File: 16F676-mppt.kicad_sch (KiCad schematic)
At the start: 50 parts, among them J1 S+, J2 S-, J3 VB+, J4 VB-, Q1 BUK9511-55A127, Q2 BUK9511-55A127, Q3 2N2222A, Q4 2N2222A, Q5 2N2907A, Q6 2N2222A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

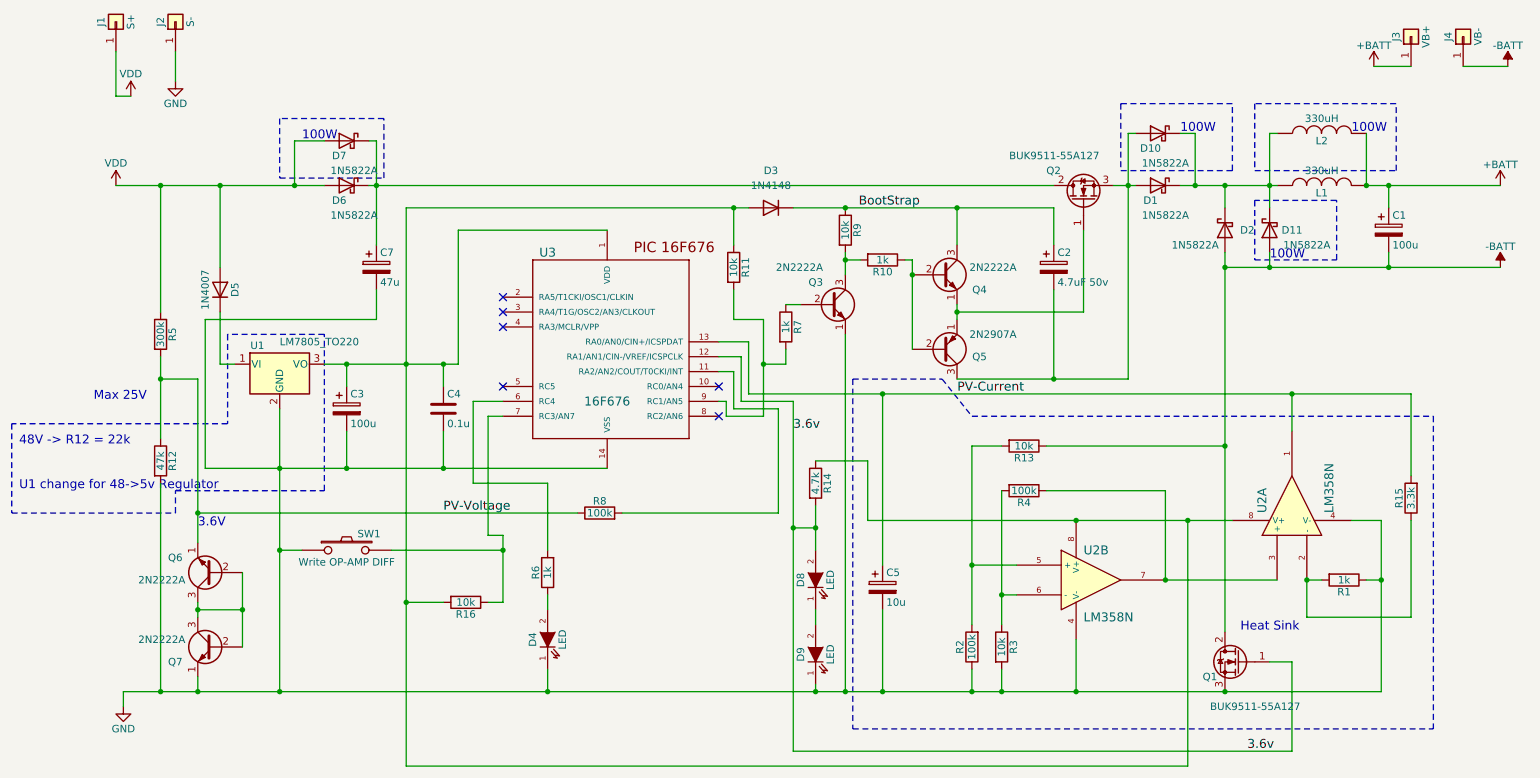
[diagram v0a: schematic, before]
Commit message: Add optional external xtal.
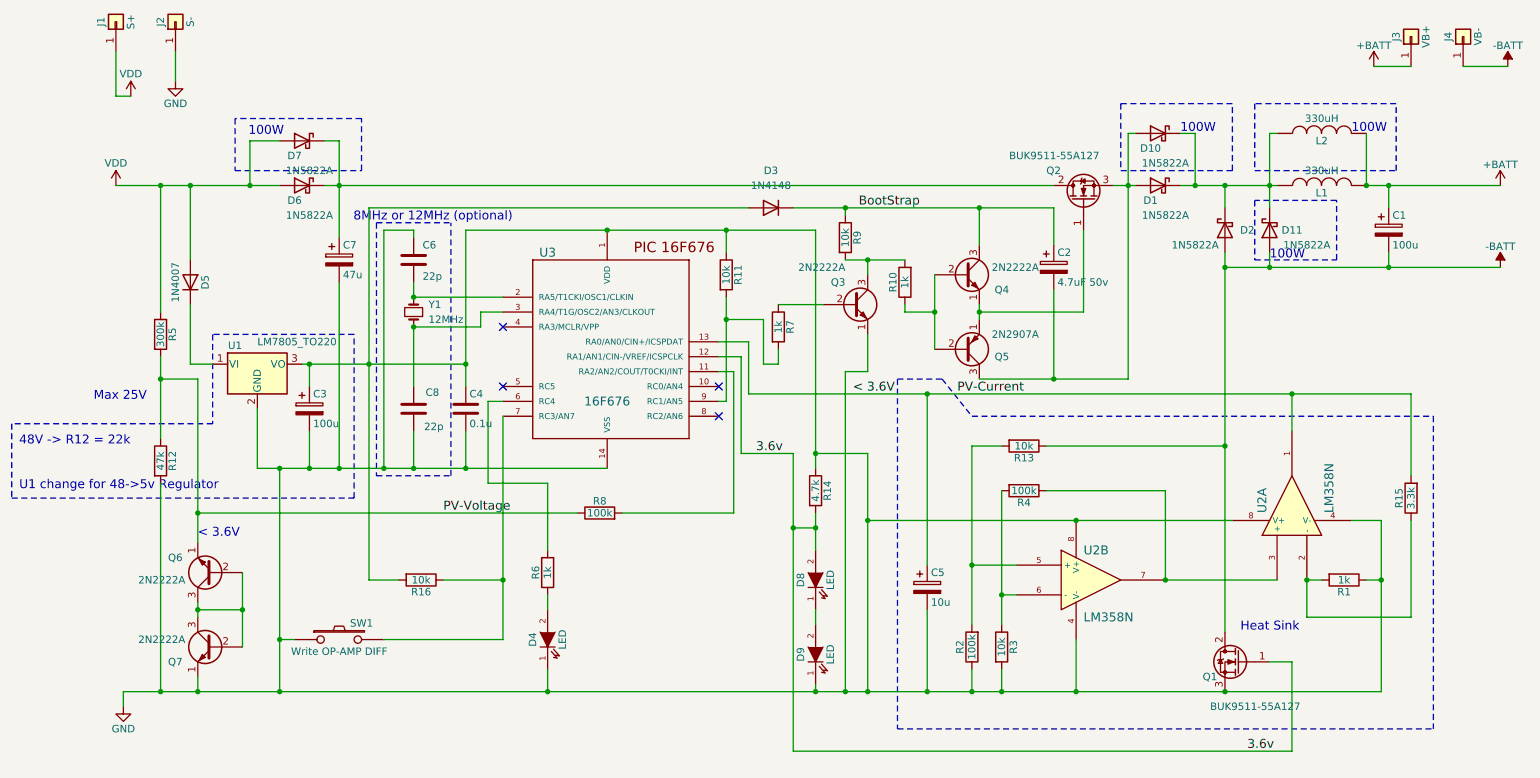
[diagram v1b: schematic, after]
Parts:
- added C6, C8: 22p, symbol Device:C
- added Y1: 12MHz, symbol Device:Crystal_Small
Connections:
- net GND: now also C3.1, C4.1, D3.2 (A), R11.1, R14.1, R16.2, U1.3 (VO), U2.8 (V+), U2.8 (V+), U3.1 (VDD), C6.1, C8.2
- net at U3.2 (RA5/T1CKI/OSC1/CLKIN): now also C6.2, Y1.2
- net at U3.3 (RA4/T1G/OSC2/AN3/CLKOUT): now also C8.1, Y1.1
- net PV-Current renamed < 3.6V
- no-connect marks 6 -> 4
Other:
- note added: "8MHz or 12MHz (optional)"
- note added: "< 3.6V"
- note removed: "3.6V"
- moved on the sheet: C3, C4, C5, C7, D5, D6, D7, Q3, Q4, Q5, R10, R11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

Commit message: Update SCH and PCB files.
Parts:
- added D12: BZX79C12, Diode_THT:D_DO-35_SOD27_P2.54mm_Vertical_AnodeUp, symbol Device:D_Zener
- C2, C3, C5: footprint Capacitors_THT:CP_Radial_D12.5mm_P5.00mm -> Capacitor_THT:CP_Radial_D8.0mm_P2.50mm
- C6, C8: footprint (none) -> Capacitor_THT:C_Rect_L4.6mm_W2.0mm_P2.50mm_MKS02_FKP02
- Y1: footprint (none) -> Crystal:Crystal_HC49-U_Vertical
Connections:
- net GND: no longer C3.1, C4.1, D3.2 (A), R11.1, R14.1, R16.2, U1.3 (VO), U2.8 (V+), U2.8 (V+), U3.1 (VDD)
- net at Q2.1 (G), Q4.1 (E), Q5.1 (E): now also D12.1 (K)
- net at C2.2, D1.2 (A), D10.2 (A)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: now also D12.2 (A)
- new net: C3.1, C4.1, D3.2 (A), R11.1, R14.1, R16.2, U1.3 (VO), U2.8 (V+), U2.8 (V+), U3.1 (VDD)
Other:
- moved on the sheet: C7, SW1
